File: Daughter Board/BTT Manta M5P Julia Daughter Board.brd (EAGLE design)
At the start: 50.5 x 80.3 mm, 42 parts, among them K1 68612014422, X10 JST-XH-03-PIN-LONG-PAD, X11 Z_LIM, X2 EXTRUDER MOTOR, X3 BED THM, X4 24V, X5 24V, X6 24V, X7 24V, X8 JST-XH-03-PIN-LONG-PAD

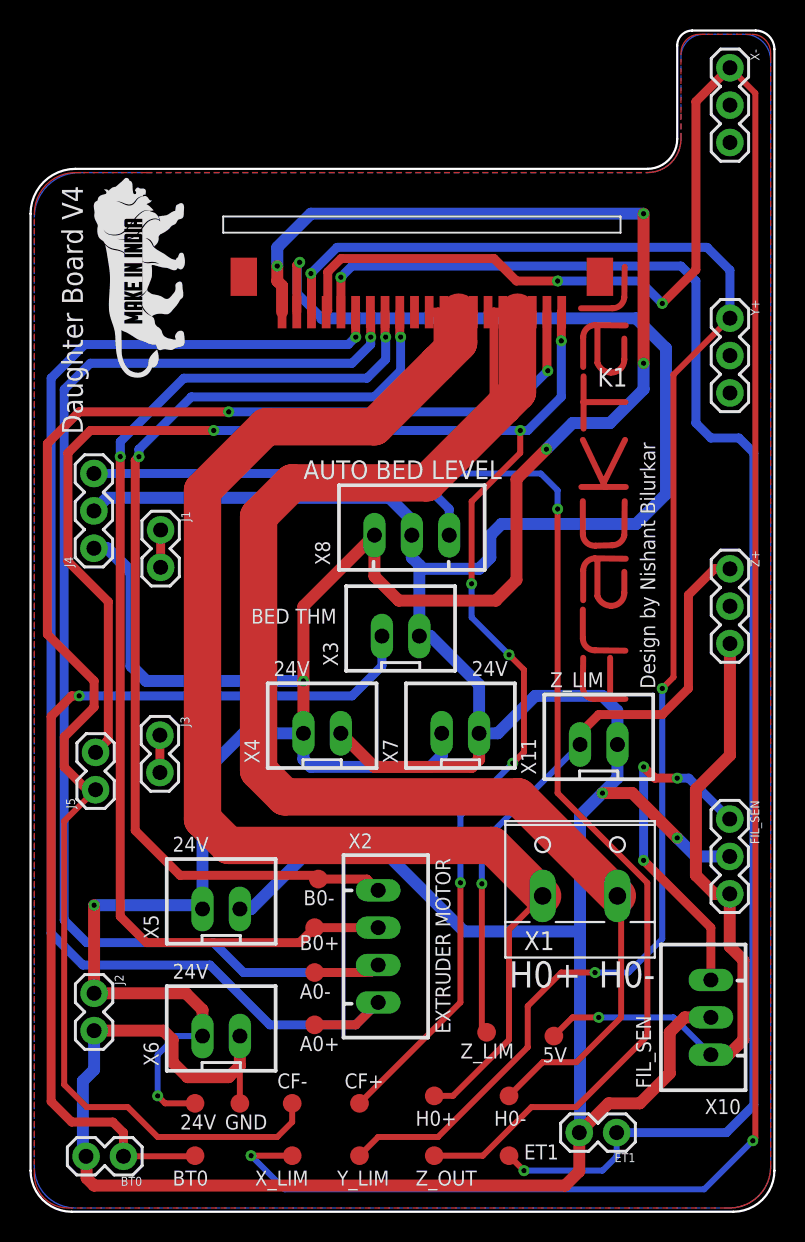
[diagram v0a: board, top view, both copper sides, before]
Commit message: Changed Probe pin voltage to 5V
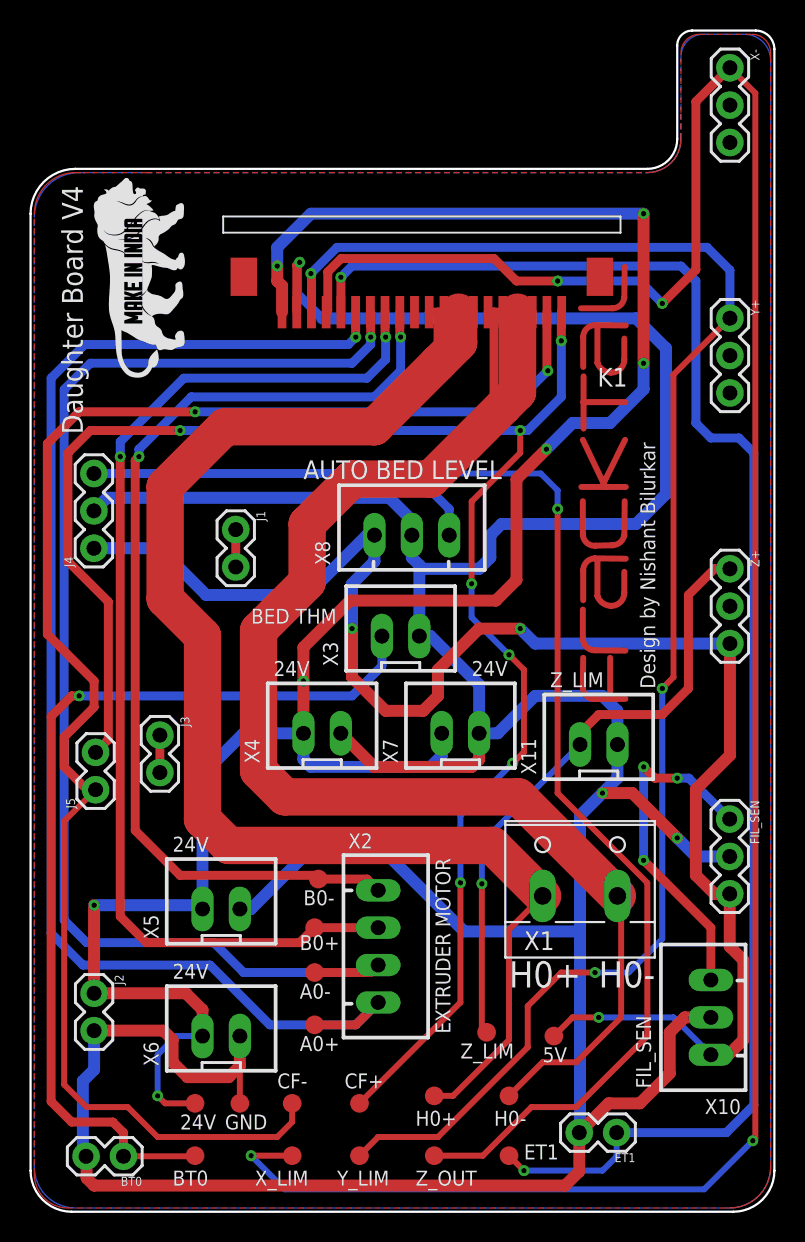
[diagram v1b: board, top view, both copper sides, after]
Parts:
- moved J1 5.11 mm to (16.5, 55.2)
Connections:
- net 24V: no longer J4.1, X8.1
- net 5V: now also J4.1, X8.1
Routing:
- net 5V: track 44.7 -> 107.5 mm, vias 1 -> 3
- net 24V: track 173.8 -> 145.1 mm
- net H0+: track 95.1 -> 98.9 mm
- net H0-: track 99.6 -> 97.3 mm
